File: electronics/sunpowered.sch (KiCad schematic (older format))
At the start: 21 parts, among them IC1 ACS713, P1 CONN_01X02, P2 CONN_02X04, Q1 PSMN0R9-30YLD, SW1 DPST, T1 12A

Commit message: flags to satisfy ERC
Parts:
- added P3: CONN_01X02, symbol CONN_01X02
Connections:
- net labels removed: GND, VCC
- wire segments 62 -> 51
- no-connect marks 0 -> 2
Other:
- moved on the sheet: C1

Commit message: started assigning footprints for the input protection board
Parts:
- JP1: footprint (none) -> Pin_Headers:Pin_Header_Straight_1x03
- P2: footprint (none) -> Pin_Headers:Pin_Header_Straight_2x04
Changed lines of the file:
@@
 F 0 "D2" V 6900 2100 50  0000 C CNN
 F 1 "24V" V 6800 2100 50  0000 C CNN
-F 2 "" H 6900 2000 60  0000 C CNN
+F 2 "" H 6900 2000 60  0001 C CNN
 F 3 "http://www.mccsemi.com/up_pdf/MMSZ5221-MMSZ5259%28SOD123%29.pdf" H 6900 2000 60  0001 C CNN
 F 4 "~" V 7000 1650 39  0000 C CNN "Note"
@@
 F 0 "F1" H 4400 1600 50  0000 C CNN
 F 1 "8A" H 4200 1500 50  0000 C CNN
-F 2 "" H 4300 1550 60  0000 C CNN
+F 2 "" H 4300 1550 60  0001 C CNN
 F 3 "" H 4300 1550 60  0000 C CNN
 	1    4300 1550
@@
 F 0 "C3" H 6550 2400 50  0000 L CNN
 F 1 "100n" H 6550 2200 50  0000 L CNN
-F 2 "" H 6538 2150 30  0000 C CNN
+F 2 "" H 6538 2150 30  0001 C CNN
 F 3 "" H 6500 2300 60  0000 C CNN
 	1    6500 2300
@@
 F 0 "R2" H 7000 2450 50  0000 C CNN
 F 1 "1k" V 6907 2651 50  0000 C CNN
-F 2 "" V 6830 2650 30  0000 C CNN
+F 2 "" V 6830 2650 30  0001 C CNN
 F 3 "" H 6900 2650 30  0000 C CNN
 	1    6900 2650
@@
 F 0 "C4" H 7300 2800 50  0000 L CNN
 F 1 "47n" H 7300 2600 50  0000 L CNN
-F 2 "" H 7288 2550 30  0000 C CNN
+F 2 "" H 7288 2550 30  0001 C CNN
 F 3 "" H 7250 2700 60  0000 C CNN
 	1    7250 2700
@@
 F 0 "T1" V 7650 2350 50  0000 C CNN
 F 1 "12A" V 7650 2100 50  0000 C CNN
-F 2 "" H 7650 2250 60  0000 C CNN
+F 2 "" H 7650 2250 60  0001 C CNN
 F 3 "http://www.nxp.com/documents/data_sheet/BT151S_SER_L_R.pdf" H 7650 2250 60  0001 C CNN
 	1    7650 2250
@@
 F 0 "D3" H 8200 1650 50  0000 C CNN
 F 1 "12A" H 8200 1450 50  0000 C CNN
-F 2 "" H 8200 1550 60  0000 C CNN
+F 2 "" H 8200 1550 60  0001 C CNN
 F 3 "http://www.vishay.com/docs/89094/v12p12.pdf" H 8200 1550 60  0001 C CNN
 	1    8200 1550
@@
 F 0 "D1" V 6250 2100 50  0000 C CNN
 F 1 "23V" V 6150 2100 50  0000 C CNN
-F 2 "" H 6250 2000 60  0000 C CNN
+F 2 "" H 6250 2000 60  0001 C CNN
 F 3 "" H 6250 2000 60  0000 C CNN
 	1    6250 2000
@@
 F 0 "Q1" H 9250 2250 50  0000 R CNN
 F 1 "PSMN0R9-30YLD" V 9500 2650 50  0000 R CNN
-F 2 "" H 9300 2400 60  0000 C CNN
+F 2 "" H 9300 2400 60  0001 C CNN
 F 3 "http://www.nxp.com/documents/data_sheet/PSMN0R9-30YLD.pdf" H 9300 2400 60  0001 C CNN
 	1    9300 2400
@@
 F 0 "R3" H 8700 2550 50  0000 C CNN
 F 1 "10k" V 8607 2651 50  0000 C CNN
-F 2 "" V 8530 2650 30  0000 C CNN
+F 2 "" V 8530 2650 30  0001 C CNN
 F 3 "" H 8600 2650 30  0000 C CNN
 	1    8600 2650
@@
 F 0 "R4" V 8750 2400 50  0000 C CNN
 F 1 "1k" V 8857 2401 50  0000 C CNN
-F 2 "" V 8780 2400 30  0000 C CNN
+F 2 "" V 8780 2400 30  0001 C CNN
 F 3 "" H 8850 2400 30  0000 C CNN
 	1    8850 2400
@@
 F 0 "C1" H 4700 2250 50  0000 L CNN
 F 1 "0.1u" H 4350 2250 50  0000 L CNN
-F 2 "" H 4638 2100 30  0000 C CNN
+F 2 "" H 4638 2100 30  0001 C CNN
 F 3 "" H 4600 2250 60  0000 C CNN
 	1    4600 2250
@@
 F 0 "SW1" H 3600 2450 50  0000 C CNN
 F 1 "DPST" H 3600 2350 50  0001 C CNN
-F 2 "" H 3300 2400 60  0000 C CNN
+F 2 "" H 3300 2400 60  0001 C CNN
 F 3 "" H 3300 2400 60  0000 C CNN
 	1    3300 2400
@@
 F 0 "C2" V 5500 2450 50  0000 L CNN
 F 1 "47n" V 5500 2200 50  0000 L CNN
-F 2 "" H 5488 2250 30  0000 C CNN
+F 2 "" H 5488 2250 30  0001 C CNN
 F 3 "" H 5450 2400 60  0000 C CNN
 	1    5450 2400
@@
 F 0 "R1" V 4330 1950 50  0000 C CNN
 F 1 "220" V 4257 1951 50  0000 C CNN
-F 2 "" V 4180 1950 30  0000 C CNN
+F 2 "" V 4180 1950 30  0001 C CNN
 F 3 "" H 4250 1950 30  0000 C CNN
 	1    4250 1950
@@
 F 0 "P1" H 2600 2550 50  0000 C CNN
 F 1 "CONN_01X02" V 2700 2400 50  0000 C CNN
-F 2 "" H 2600 2400 60  0000 C CNN
+F 2 "" H 2600 2400 60  0001 C CNN
 F 3 "" H 2600 2400 60  0000 C CNN
 	1    2600 2400
@@
 F 0 "JP1" H 8450 2300 50  0000 L CNN
 F 1 "JUMPER3" H 8400 2500 50  0001 C BNN
-F 2 "" H 8400 2400 60  0000 C CNN
+F 2 "Pin_Headers:Pin_Header_Straight_1x03" H 8400 2400 60  0001 C CNN
 F 3 "" H 8400 2400 60  0000 C CNN
 	1    8400 2400
@@
 F 0 "R5" H 8500 1800 50  0000 C CNN
 F 1 "5k" V 8407 1801 50  0000 C CNN
-F 2 "" V 8330 1800 30  0000 C CNN
+F 2 "" V 8330 1800 30  0001 C CNN
 F 3 "" H 8400 1800 30  0000 C CNN
 	1    8400 1800
@@
 F 0 "P2" H 3500 4300 50  0000 C CNN
 F 1 "CONN_02X04" H 3500 3800 50  0000 C CNN
-F 2 "" H 3500 2850 60  0000 C CNN
+F 2 "Pin_Headers:Pin_Header_Straight_2x04" H 3500 2850 60  0001 C CNN
 F 3 "" H 3500 2850 60  0000 C CNN
 	1    3500 4050
@@
 F 0 "C5" V 4200 4200 50  0000 L CNN
 F 1 "4700u" V 4050 3800 50  0000 L CNN
-F 2 "" H 4188 3950 30  0000 C CNN
+F 2 "" H 4188 3950 30  0001 C CNN
 F 3 "" H 4150 4100 60  0000 C CNN
 	1    4150 4100
@@
 F 0 "P3" H 9850 1750 50  0000 C CNN
 F 1 "CONN_01X02" V 9950 1600 50  0000 C CNN
-F 2 "" H 9850 1600 60  0000 C CNN
+F 2 "" H 9850 1600 60  0001 C CNN
 F 3 "" H 9850 1600 60  0000 C CNN
 	1    9850 1600

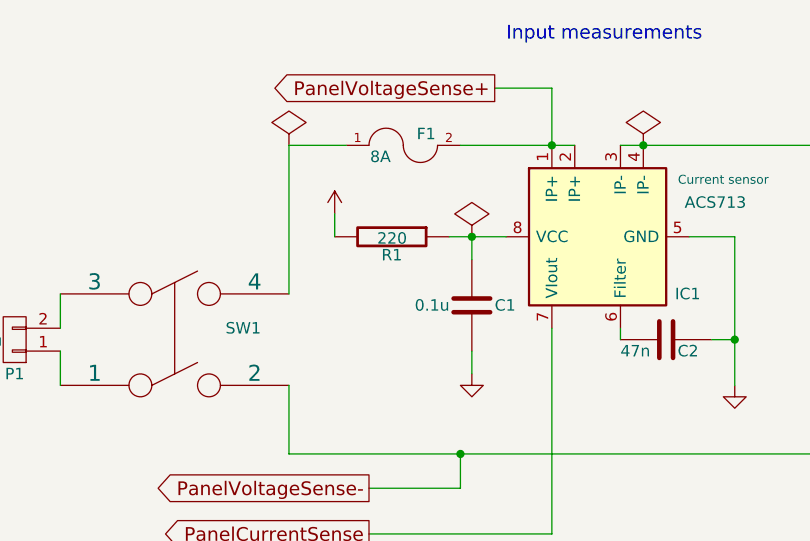
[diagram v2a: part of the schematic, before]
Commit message: assigned footprints for most passives
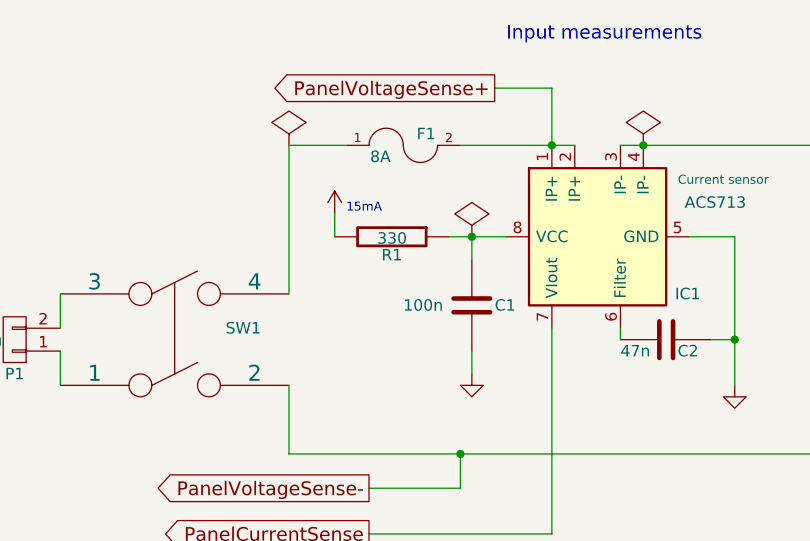
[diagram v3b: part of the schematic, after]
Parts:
- C1: value 0.1u -> 100n; footprint (none) -> Capacitors_SMD:C_0603_HandSoldering
- C2, C3, C4: footprint (none) -> Capacitors_SMD:C_0603_HandSoldering
- R1: value 220 -> 330; footprint (none) -> Resistors_SMD:R_0603_HandSoldering
- R2, R3, R4, R5: footprint (none) -> Resistors_SMD:R_0603_HandSoldering
- T1: footprint (none) -> Transistors_SMD:sot428
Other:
- note added: "15mA"
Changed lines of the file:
@@
 F 0 "C3" H 6550 2400 50  0000 L CNN
 F 1 "100n" H 6550 2200 50  0000 L CNN
-F 2 "" H 6538 2150 30  0001 C CNN
+F 2 "Capacitors_SMD:C_0603_HandSoldering" H 6538 2150 30  0001 C CNN
 F 3 "" H 6500 2300 60  0000 C CNN
 	1    6500 2300
@@
 F 0 "R2" H 7000 2450 50  0000 C CNN
 F 1 "1k" V 6907 2651 50  0000 C CNN
-F 2 "" V 6830 2650 30  0001 C CNN
+F 2 "Resistors_SMD:R_0603_HandSoldering" V 6830 2650 30  0001 C CNN
 F 3 "" H 6900 2650 30  0000 C CNN
 	1    6900 2650
@@
 F 0 "C4" H 7300 2800 50  0000 L CNN
 F 1 "47n" H 7300 2600 50  0000 L CNN
-F 2 "" H 7288 2550 30  0001 C CNN
+F 2 "Capacitors_SMD:C_0603_HandSoldering" H 7288 2550 30  0001 C CNN
 F 3 "" H 7250 2700 60  0000 C CNN
 	1    7250 2700
@@
 F 0 "T1" V 7650 2350 50  0000 C CNN
 F 1 "12A" V 7650 2100 50  0000 C CNN
-F 2 "" H 7650 2250 60  0001 C CNN
+F 2 "Transistors_SMD:sot428" H 7650 2250 60  0001 C CNN
 F 3 "http://www.nxp.com/documents/data_sheet/BT151S_SER_L_R.pdf" H 7650 2250 60  0001 C CNN
 	1    7650 2250
@@
 F 0 "R3" H 8700 2550 50  0000 C CNN
 F 1 "10k" V 8607 2651 50  0000 C CNN
-F 2 "" V 8530 2650 30  0001 C CNN
+F 2 "Resistors_SMD:R_0603_HandSoldering" V 8530 2650 30  0001 C CNN
 F 3 "" H 8600 2650 30  0000 C CNN
 	1    8600 2650
@@
 F 0 "R4" V 8750 2400 50  0000 C CNN
 F 1 "1k" V 8857 2401 50  0000 C CNN
-F 2 "" V 8780 2400 30  0001 C CNN
+F 2 "Resistors_SMD:R_0603_HandSoldering" V 8780 2400 30  0001 C CNN
 F 3 "" H 8850 2400 30  0000 C CNN
 	1    8850 2400
@@
 P 4600 2250
 F 0 "C1" H 4700 2250 50  0000 L CNN
-F 1 "0.1u" H 4350 2250 50  0000 L CNN
-F 2 "" H 4638 2100 30  0001 C CNN
+F 1 "100n" H 4300 2250 50  0000 L CNN
+F 2 "Capacitors_SMD:C_0603_HandSoldering" H 4638 2100 30  0001 C CNN
 F 3 "" H 4600 2250 60  0000 C CNN
 	1    4600 2250
@@
 F 0 "C2" V 5500 2450 50  0000 L CNN
 F 1 "47n" V 5500 2200 50  0000 L CNN
-F 2 "" H 5488 2250 30  0001 C CNN
+F 2 "Capacitors_SMD:C_0603_HandSoldering" H 5488 2250 30  0001 C CNN
 F 3 "" H 5450 2400 60  0000 C CNN
 	1    5450 2400
@@
 P 4250 1950
 F 0 "R1" V 4330 1950 50  0000 C CNN
-F 1 "220" V 4257 1951 50  0000 C CNN
-F 2 "" V 4180 1950 30  0001 C CNN
+F 1 "330" V 4257 1951 50  0000 C CNN
+F 2 "Resistors_SMD:R_0603_HandSoldering" V 4180 1950 30  0001 C CNN
 F 3 "" H 4250 1950 30  0000 C CNN
 	1    4250 1950
@@
 F 0 "R5" H 8500 1800 50  0000 C CNN
 F 1 "5k" V 8407 1801 50  0000 C CNN
-F 2 "" V 8330 1800 30  0001 C CNN
+F 2 "Resistors_SMD:R_0603_HandSoldering" V 8330 1800 30  0001 C CNN
 F 3 "" H 8400 1800 30  0000 C CNN
 	1    8400 1800
@@
 	1    0    0    -1
 $EndComp
+Text Notes 4050 1850 0    39   ~ 0
+15mA
 $EndSCHEMATC

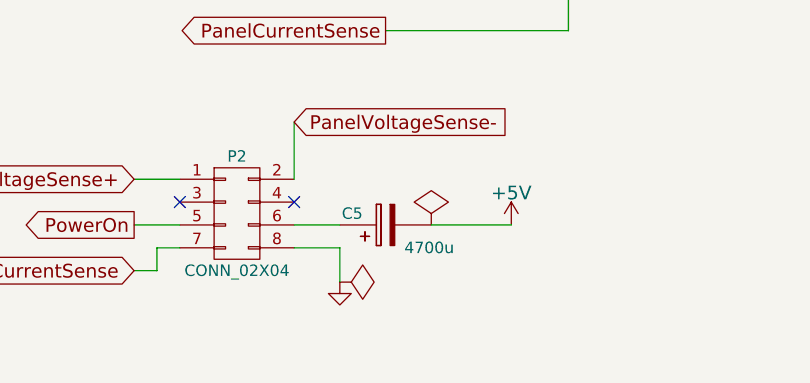
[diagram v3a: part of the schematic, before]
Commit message: corrected filter cap position [lol]
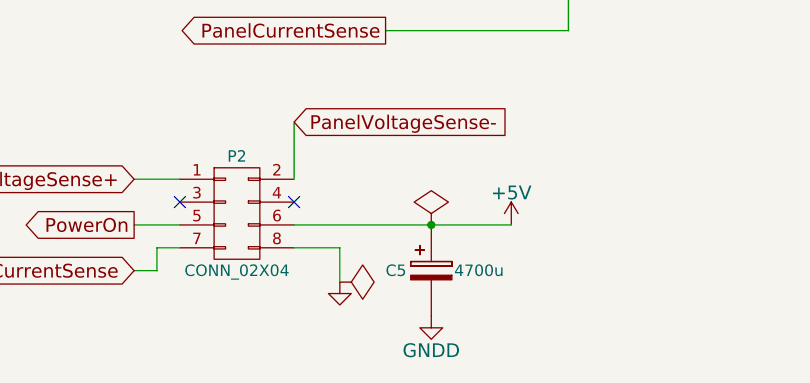
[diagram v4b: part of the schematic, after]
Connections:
- net +5V: now also C5.1, P2.6 (P6); no longer C5.2
- net GNDD: now also C5.2
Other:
- moved on the sheet: C5
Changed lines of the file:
@@
 L CP2 C5
 U 1 1 54E900DF
-P 4150 4100
-F 0 "C5" V 4200 4200 50  0000 L CNN
-F 1 "4700u" V 4050 3800 50  0000 L CNN
-F 2 "" H 4188 3950 30  0001 C CNN
-F 3 "" H 4150 4100 60  0000 C CNN
-	1    4150 4100
-	0    -1   -1   0
+P 4350 4300
+F 0 "C5" H 4150 4300 50  0000 L CNN
+F 1 "4700u" H 4450 4300 50  0000 L CNN
+F 2 "" H 4388 4150 30  0001 C CNN
+F 3 "" H 4350 4300 60  0000 C CNN
+	1    4350 4300
+	1    0    0    -1
 $EndComp
 $Comp
@@
 	3050 4100 3250 4100
 Wire Wire Line
-	3950 4100 3750 4100
+	3750 4100 4700 4100
 Wire Wire Line
 	3050 4300 3150 4300
@@
 Connection ~ 4600 1950
 Wire Wire Line
-	4700 4100 4350 4100
-Wire Wire Line
 	4000 1850 4000 1950
 $Comp
 L PWR_FLAG #FLG08
+U 1 1 54E96C83
+P 4350 4100
+F 0 "#FLG08" H 4350 4195 30  0001 C CNN
+F 1 "PWR_FLAG" H 4350 4280 30  0001 C CNN
+F 2 "" H 4350 4100 60  0000 C CNN
+F 3 "" H 4350 4100 60  0000 C CNN
+	1    4350 4100
+	1    0    0    -1
+$EndComp
+$Comp
+L PWR_FLAG #FLG09
+U 1 1 54E92590
+P 3800 1550
+F 0 "#FLG09" H 3800 1645 30  0001 C CNN
+F 1 "PWR_FLAG" H 3800 1730 30  0001 C CNN
+F 2 "" H 3800 1550 60  0000 C CNN
+F 3 "" H 3800 1550 60  0000 C CNN
+	1    3800 1550
+	1    0    0    -1
+$EndComp
+Text Notes 4050 1850 0    39   ~ 0
+15mA
+Connection ~ 4350 4100
+$Comp
+L GNDD #PWR010
+U 1 1 54E9AC18
+P 4350 4500
+F 0 "#PWR010" H 4350 4250 60  0001 C CNN
+F 1 "GNDD" H 4350 4350 60  0000 C CNN
+F 2 "" H 4350 4500 60  0000 C CNN
+F 3 "" H 4350 4500 60  0000 C CNN
+	1    4350 4500
+	1    0    0    -1
+$EndComp
+$Comp
+L PWR_FLAG #FLG011
 U 1 1 54E96236
 P 4600 1950
-F 0 "#FLG08" H 4600 2045 30  0001 C CNN
+F 0 "#FLG011" H 4600 2045 30  0001 C CNN
 F 1 "PWR_FLAG" H 4600 2130 30  0001 C CNN
 F 2 "" H 4600 1950 60  0000 C CNN
@@
 	1    0    0    -1
 $EndComp
-$Comp
-L PWR_FLAG #FLG09
-U 1 1 54E96C83
-P 4350 4100
-F 0 "#FLG09" H 4350 4195 30  0001 C CNN
-F 1 "PWR_FLAG" H 4350 4280 30  0001 C CNN
-F 2 "" H 4350 4100 60  0000 C CNN
-F 3 "" H 4350 4100 60  0000 C CNN
-	1    4350 4100
-	1    0    0    -1
-$EndComp
-$Comp
-L PWR_FLAG #FLG010
-U 1 1 54E92590
-P 3800 1550
-F 0 "#FLG010" H 3800 1645 30  0001 C CNN
-F 1 "PWR_FLAG" H 3800 1730 30  0001 C CNN
-F 2 "" H 3800 1550 60  0000 C CNN
-F 3 "" H 3800 1550 60  0000 C CNN
-	1    3800 1550
-	1    0    0    -1
-$EndComp
-Text Notes 4050 1850 0    39   ~ 0
-15mA
 $EndSCHEMATC

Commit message: removed lower protection zener as it's hard to get, added footprints for the crowbar circuit components
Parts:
- removed D1: 23V, symbol ZENER
- D1: renamed from D2; footprint (none) -> Diodes_SMD:Diode-SMC_Handsoldering
- renumbered C5 to C1, C1 to C2, C2 to C3, C3 to C4, C4 to C5, D3 to D2, R5 to R3, R3 to R4, R4 to R5
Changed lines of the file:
@@
 $EndDescr
 $Comp
-L ZENER D2
+L ZENER D1
 U 1 1 54D52D0F
 P 6900 2000
-F 0 "D2" V 6900 2100 50  0000 C CNN
+F 0 "D1" V 6900 2100 50  0000 C CNN
 F 1 "24V" V 6800 2100 50  0000 C CNN
-F 2 "" H 6900 2000 60  0001 C CNN
-F 3 "http://www.mccsemi.com/up_pdf/MMSZ5221-MMSZ5259%28SOD123%29.pdf" H 6900 2000 60  0001 C CNN
+F 2 "Diodes_SMD:Diode-SMC_Handsoldering" H 6900 2000 60  0001 C CNN
+F 3 "http://www.comchiptech.com/cms/UserFiles/ACZRC5333B-G%20Thru.%20ACZRC5388B-G%20RevA.pdf" H 6900 2000 60  0001 C CNN
 F 4 "~" V 7000 1650 39  0000 C CNN "Note"
 	1    6900 2000
@@
 $EndComp
 $Comp
-L C C3
+L C C4
 U 1 1 54D539D0
 P 6500 2300
-F 0 "C3" H 6550 2400 50  0000 L CNN
+F 0 "C4" H 6550 2400 50  0000 L CNN
 F 1 "100n" H 6550 2200 50  0000 L CNN
 F 2 "Capacitors_SMD:C_0603_HandSoldering" H 6538 2150 30  0001 C CNN
@@
 $EndComp
 $Comp
-L C C4
+L C C5
 U 1 1 54D53D1F
 P 7250 2700
-F 0 "C4" H 7300 2800 50  0000 L CNN
+F 0 "C5" H 7300 2800 50  0000 L CNN
 F 1 "47n" H 7300 2600 50  0000 L CNN
 F 2 "Capacitors_SMD:C_0603_HandSoldering" H 7288 2550 30  0001 C CNN
@@
 $EndComp
 $Comp
-L DIODESCH D3
+L DIODESCH D2
 U 1 1 54D53FCE
 P 8200 1550
-F 0 "D3" H 8200 1650 50  0000 C CNN
+F 0 "D2" H 8200 1650 50  0000 C CNN
 F 1 "12A" H 8200 1450 50  0000 C CNN
 F 2 "" H 8200 1550 60  0001 C CNN
@@
 	1    8200 1550
 	1    0    0    -1
-$EndComp
-$Comp
-L ZENER D1
-U 1 1 54D5E43B
-P 6250 2000
-F 0 "D1" V 6250 2100 50  0000 C CNN
-F 1 "23V" V 6150 2100 50  0000 C CNN
-F 2 "" H 6250 2000 60  0001 C CNN
-F 3 "" H 6250 2000 60  0000 C CNN
-	1    6250 2000
-	0    -1   -1   0
 $EndComp
 $Comp
@@
 $EndComp
 $Comp
-L R R3
+L R R4
 U 1 1 54D70FF3
 P 8600 2650
-F 0 "R3" H 8700 2550 50  0000 C CNN
+F 0 "R4" H 8700 2550 50  0000 C CNN
 F 1 "10k" V 8607 2651 50  0000 C CNN
 F 2 "Resistors_SMD:R_0603_HandSoldering" V 8530 2650 30  0001 C CNN
@@
 $EndComp
 $Comp
-L R R4
+L R R5
 U 1 1 54D7146D
 P 8850 2400
-F 0 "R4" V 8750 2400 50  0000 C CNN
+F 0 "R5" V 8750 2400 50  0000 C CNN
 F 1 "1k" V 8857 2401 50  0000 C CNN
 F 2 "Resistors_SMD:R_0603_HandSoldering" V 8780 2400 30  0001 C CNN
@@
 $EndComp
 $Comp
-L C C1
+L C C2
 U 1 1 54D74223
 P 4600 2250
-F 0 "C1" H 4700 2250 50  0000 L CNN
+F 0 "C2" H 4700 2250 50  0000 L CNN
 F 1 "100n" H 4300 2250 50  0000 L CNN
 F 2 "Capacitors_SMD:C_0603_HandSoldering" H 4638 2100 30  0001 C CNN
@@
 $EndComp
 $Comp
-L C C2
+L C C3
 U 1 1 54D76924
 P 5450 2400
-F 0 "C2" V 5500 2450 50  0000 L CNN
+F 0 "C3" V 5500 2450 50  0000 L CNN
 F 1 "47n" V 5500 2200 50  0000 L CNN
 F 2 "Capacitors_SMD:C_0603_HandSoldering" H 5488 2250 30  0001 C CNN
@@
 $EndComp
 $Comp
-L R R5
+L R R3
 U 1 1 54E8C723
 P 8400 1800
-F 0 "R5" H 8500 1800 50  0000 C CNN
+F 0 "R3" H 8500 1800 50  0000 C CNN
 F 1 "5k" V 8407 1801 50  0000 C CNN
 F 2 "Resistors_SMD:R_0603_HandSoldering" V 8330 1800 30  0001 C CNN
@@
 $EndComp
 $Comp
-L CP2 C5
+L CP2 C1
 U 1 1 54E900DF
 P 4350 4300
-F 0 "C5" H 4150 4300 50  0000 L CNN
+F 0 "C1" H 4150 4300 50  0000 L CNN
 F 1 "4700u" H 4450 4300 50  0000 L CNN
 F 2 "" H 4388 4150 30  0001 C CNN
@@
 Connection ~ 6500 1550
 Wire Wire Line
-	6250 2900 6250 2200
-Connection ~ 6250 2900
-Wire Wire Line
 	3800 1550 3800 2200
-Connection ~ 6250 1550
 Wire Wire Line
 	9400 1900 9650 1900
@@
 Connection ~ 4950 1550
 Wire Wire Line
-	6250 1550 6250 1800
-Wire Wire Line
 	6900 1550 6900 1800

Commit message: added temporary lirbary for custom footprints, to be exported to public KiCad's later
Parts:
- C1: footprint (none) -> Capacitors_ThroughHole:Capacitor5x11RM2.5
- D2: footprint (none) -> Diodes_SMD:Diode-SMC_Handsoldering
- F1: footprint (none) -> Fuse_Holders_and_Fuses:Fuseholder5x20_horiz_open_universal_Type-III
- P1, P3: footprint (none) -> Terminal_Blocks:TerminalBlock_WAGO-236_2Stift_RM5mm_2pol
- Q1: footprint (none) -> cyplo's:TO277A
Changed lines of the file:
@@
 F 0 "F1" H 4400 1600 50  0000 C CNN
 F 1 "8A" H 4200 1500 50  0000 C CNN
-F 2 "" H 4300 1550 60  0001 C CNN
+F 2 "Fuse_Holders_and_Fuses:Fuseholder5x20_horiz_open_universal_Type-III" H 4300 1550 60  0001 C CNN
 F 3 "" H 4300 1550 60  0000 C CNN
 	1    4300 1550
@@
 F 0 "D2" H 8200 1650 50  0000 C CNN
 F 1 "12A" H 8200 1450 50  0000 C CNN
-F 2 "" H 8200 1550 60  0001 C CNN
+F 2 "Diodes_SMD:Diode-SMC_Handsoldering" H 8200 1550 60  0001 C CNN
 F 3 "http://www.vishay.com/docs/89094/v12p12.pdf" H 8200 1550 60  0001 C CNN
 	1    8200 1550
@@
 F 0 "Q1" H 9250 2250 50  0000 R CNN
 F 1 "PSMN0R9-30YLD" V 9500 2650 50  0000 R CNN
-F 2 "" H 9300 2400 60  0001 C CNN
+F 2 "cyplo's:TO277A" H 9300 2400 60  0001 C CNN
 F 3 "http://www.nxp.com/documents/data_sheet/PSMN0R9-30YLD.pdf" H 9300 2400 60  0001 C CNN
 	1    9300 2400
@@
 F 0 "P1" H 2600 2550 50  0000 C CNN
 F 1 "CONN_01X02" V 2700 2400 50  0000 C CNN
-F 2 "" H 2600 2400 60  0001 C CNN
+F 2 "Terminal_Blocks:TerminalBlock_WAGO-236_2Stift_RM5mm_2pol" H 2600 2400 60  0001 C CNN
 F 3 "" H 2600 2400 60  0000 C CNN
 	1    2600 2400
@@
 F 0 "C1" H 4150 4300 50  0000 L CNN
 F 1 "4700u" H 4450 4300 50  0000 L CNN
-F 2 "" H 4388 4150 30  0001 C CNN
+F 2 "Capacitors_ThroughHole:Capacitor5x11RM2.5" H 4388 4150 30  0001 C CNN
 F 3 "" H 4350 4300 60  0000 C CNN
 	1    4350 4300
@@
 F 0 "P3" H 9850 1750 50  0000 C CNN
 F 1 "CONN_01X02" V 9950 1600 50  0000 C CNN
-F 2 "" H 9850 1600 60  0001 C CNN
+F 2 "Terminal_Blocks:TerminalBlock_WAGO-236_2Stift_RM5mm_2pol" H 9850 1600 60  0001 C CNN
 F 3 "" H 9850 1600 60  0000 C CNN
 	1    9850 1600

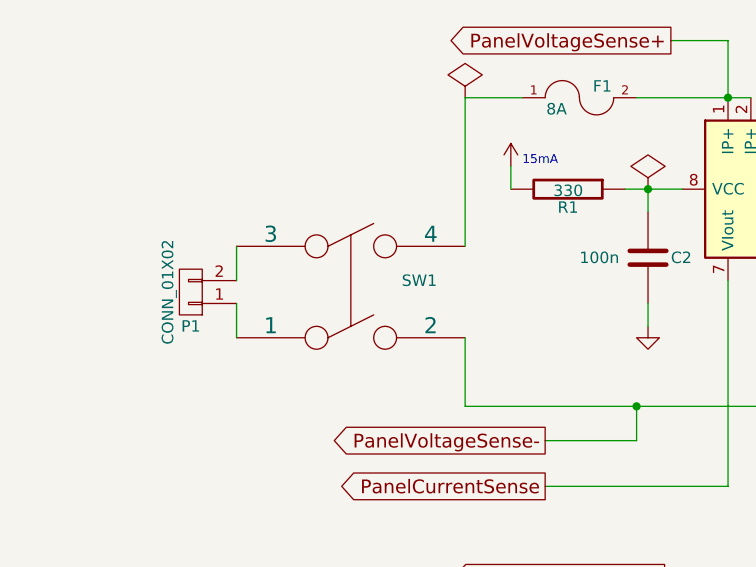
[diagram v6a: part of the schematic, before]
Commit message: all footprints added, started layout
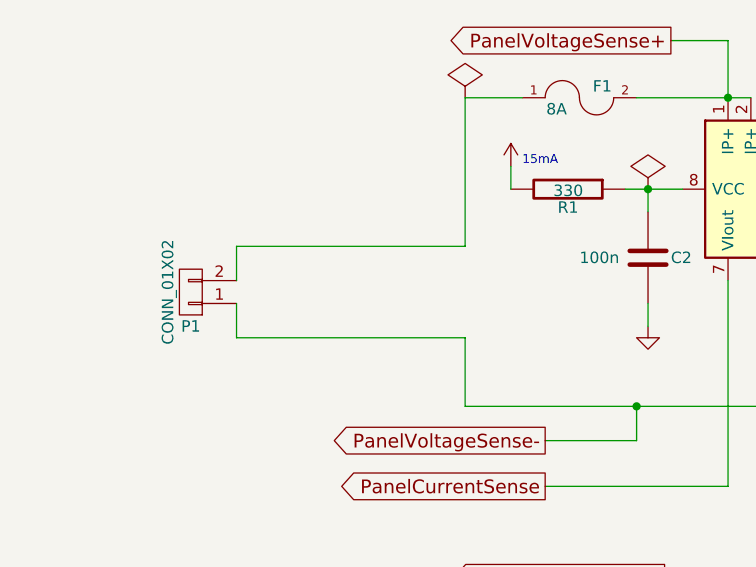
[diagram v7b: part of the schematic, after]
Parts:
- removed SW1: DPST, symbol DPST
- D2: footprint Diodes_SMD:Diode-SMC_Handsoldering -> cyplo's:TO277A
- Q1: footprint cyplo's:TO277A -> cyplo's:LFPAK56
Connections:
- net PanelVoltageSense-: now also P1.1 (P1)
- net at F1.1: now also P1.2 (P2)
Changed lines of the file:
@@
 F 0 "D2" H 8200 1650 50  0000 C CNN
 F 1 "12A" H 8200 1450 50  0000 C CNN
-F 2 "Diodes_SMD:Diode-SMC_Handsoldering" H 8200 1550 60  0001 C CNN
+F 2 "cyplo's:TO277A" H 8200 1550 60  0001 C CNN
 F 3 "http://www.vishay.com/docs/89094/v12p12.pdf" H 8200 1550 60  0001 C CNN
 	1    8200 1550
@@
 F 0 "Q1" H 9250 2250 50  0000 R CNN
 F 1 "PSMN0R9-30YLD" V 9500 2650 50  0000 R CNN
-F 2 "cyplo's:TO277A" H 9300 2400 60  0001 C CNN
+F 2 "cyplo's:LFPAK56" H 9300 2400 60  0001 C CNN
 F 3 "http://www.nxp.com/documents/data_sheet/PSMN0R9-30YLD.pdf" H 9300 2400 60  0001 C CNN
 	1    9300 2400
@@
 F 3 "" H 4600 2250 60  0000 C CNN
 	1    4600 2250
-	1    0    0    -1
-$EndComp
-$Comp
-L DPST SW1
-U 1 1 54D5CEC6
-P 3300 2400
-F 0 "SW1" H 3600 2450 50  0000 C CNN
-F 1 "DPST" H 3600 2350 50  0001 C CNN
-F 2 "" H 3300 2400 60  0001 C CNN
-F 3 "" H 3300 2400 60  0000 C CNN
-	1    3300 2400
 	1    0    0    -1
 $EndComp
@@
 	1    0    0    -1
 $EndComp
+Wire Wire Line
+	3800 2200 2800 2200
+Wire Wire Line
+	2800 2600 3800 2600
 $EndSCHEMATC
